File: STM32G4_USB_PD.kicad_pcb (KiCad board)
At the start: 2 copper layers, 34 x 24 mm, 22 parts, among them J1 USB4105-GF-A, J2 8.06.16_J-LINK_6-PIN_NEEDLE_A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, J3 Conn_01x04, J4 Conn_01x02, Q1 2N7002K, U1 STM32G431C8T6, U2 AP2205-W5-7

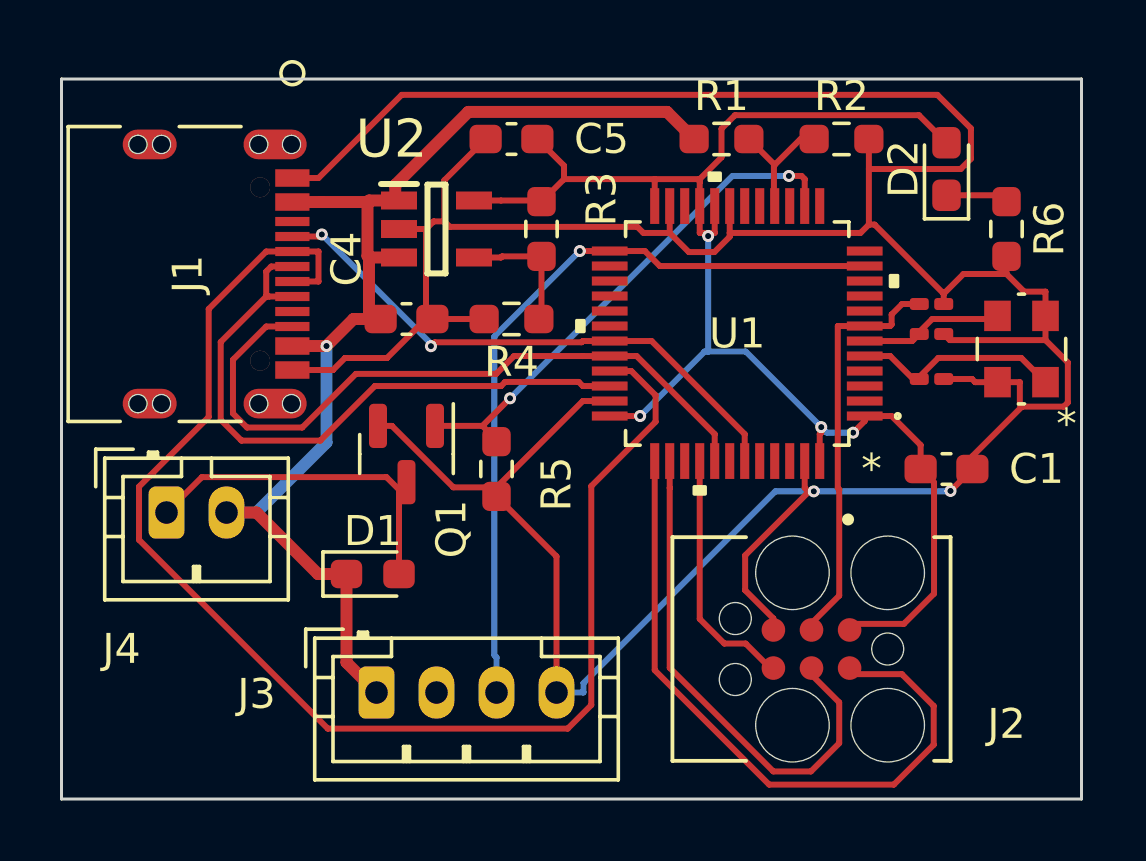
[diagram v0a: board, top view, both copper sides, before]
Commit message: Thicker Trace for VBUS
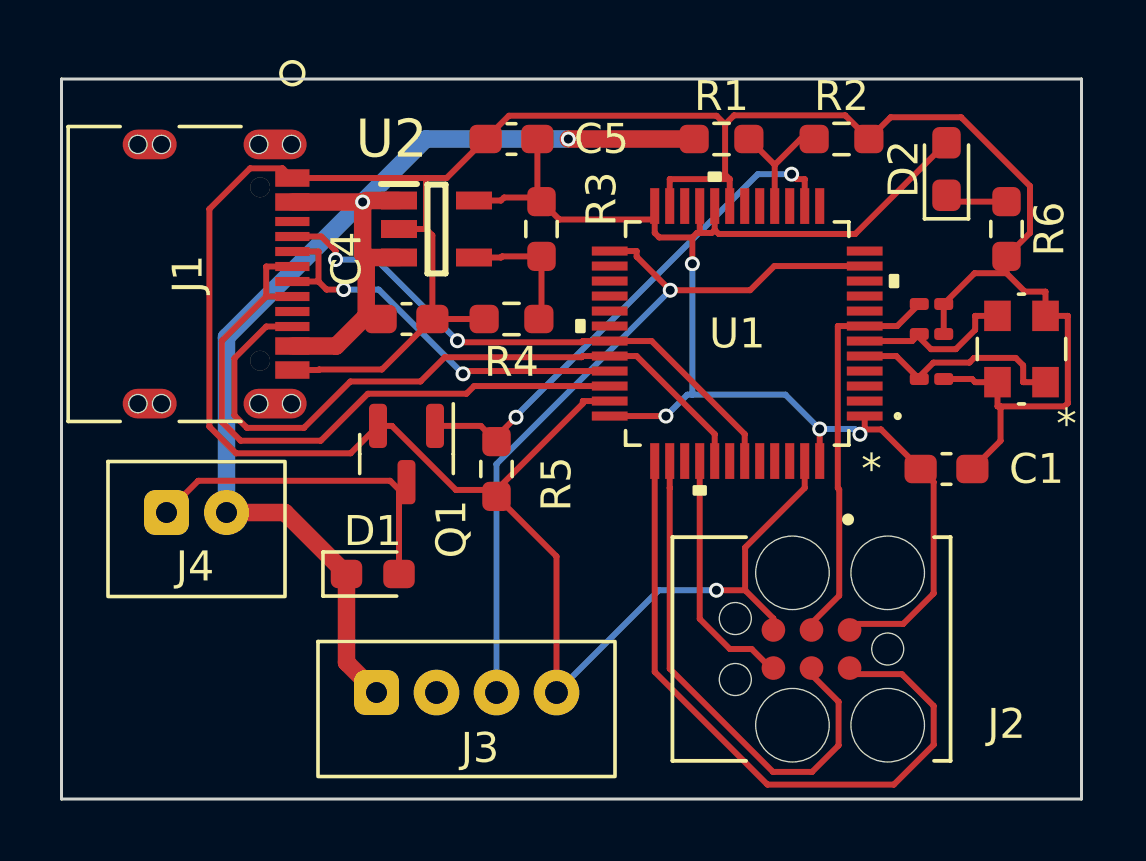
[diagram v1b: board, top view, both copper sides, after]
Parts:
- J3: footprint Connector_JST:JST_PH_B4B-PH-K_1x04_P2.00mm_Vertical -> Anh_Nguyen:JST_PH_2mm_4
- J4: footprint Connector_JST:JST_PH_B2B-PH-K_1x02_P2.00mm_Vertical -> Anh_Nguyen:JST_PH_2mm_2
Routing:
- net USB_D-: track 46.1 -> 13.8 mm, vias 0 -> 2
- net GND: track 128.7 -> 115.1 mm, vias 2 -> 1
- net V_USB: track 40.4 -> 45.3 mm, vias 1 -> 2
- net +3.3V: track 50.4 -> 48.3 mm
- net OSC_OUT: track 4.81 -> 5.50 mm

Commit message: improve VBUS trace width
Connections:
- J1 pad 13: (no net) -> GND
- J1 pad 14: (no net) -> GND
- J1 pad 15: (no net) -> GND
- J1 pad 16: (no net) -> GND
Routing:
- net V_USB: track 45.3 -> 57.0 mm, vias 2 -> 4
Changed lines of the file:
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@@
     (attr smd)
     (fp_text reference "R1" (at 0 -1.43) (layer "F.SilkS")
-      (effects (font (size 1 1) (thickness 0.15)))
+      (effects (font (size 0.5 0.5) (thickness 0.125)))
     )
     (fp_text value "20k" (at 0 1.43) (layer "F.Fab")
@@
       (effects (font (size 1 1) (thickness 0.15)))
     )
-    (fp_circle (center -6.6929 -3.4858) (end -6.3119 -3.4858) (layer "B.SilkS") (width 0.12) (fill none))
     (fp_line (start 4.9149 0.286826) (end 4.9149 -1.776026) (layer "F.SilkS") (width 0.12))
     (fp_line (start 4.9149 3.9878) (end 4.9149 2.251574) (layer "F.SilkS") (width 0.12))
@@
     (fp_line (start -4.9149 2.251574) (end -4.9149 3.9878) (layer "F.SilkS") (width 0.12))
     (fp_line (start -4.9149 3.9878) (end 4.9149 3.9878) (layer "F.SilkS") (width 0.12))
-    (fp_circle (center -6.6929 -3.4858) (end -6.3119 -3.4858) (layer "F.SilkS") (width 0.12) (fill none))
     (fp_line (start -5.069301 4.1148) (end 5.069301 4.1148) (layer "F.CrtYd") (width 0.05))
     (fp_line (start 5.069301 -4.3113) (end -5.069301 -4.3113) (layer "F.CrtYd") (width 0.05))
@@
     (fp_line (start 4.7879 3.8608) (end 4.7879 -3.8608) (layer "F.Fab") (width 0.1))
     (fp_line (start -4.7879 -3.8608) (end -4.7879 3.8608) (layer "F.Fab") (width 0.1))
-    (fp_circle (center -3.2 -5.3908) (end -2.819 -5.3908) (layer "F.Fab") (width 0.1) (fill none))
-    (pad "" np_thru_hole circle (at -4.32 0.8755 270) (size 0.6096 0.6096) (drill 0.6096) (layers *.Cu *.Mask))
-    (pad "" np_thru_hole circle (at 4.32 -3.4569 270) (size 0.6096 0.6096) (drill 0.6096) (layers *.Cu *.Mask))
-    (pad "" np_thru_hole circle (at 4.32 -2.3647 270) (size 0.6096 0.6096) (drill 0.6096) (layers *.Cu *.Mask))
-    (pad "" np_thru_hole circle (at 4.32 1.6629 270) (size 0.6096 0.6096) (drill 0.6096) (layers *.Cu *.Mask))
-    (pad "" np_thru_hole circle (at -4.32 1.6629 270) (size 0.6096 0.6096) (drill 0.6096) (layers *.Cu *.Mask))
-    (pad "" np_thru_hole circle (at 4.32 0.8755 270) (size 0.6096 0.6096) (drill 0.6096) (layers *.Cu *.Mask))
-    (pad "" np_thru_hole circle (at -4.320002 -3.4569 270) (size 0.6096 0.6096) (drill 0.6096) (layers *.Cu *.Mask))
-    (pad "" np_thru_hole circle (at -4.320002 -2.3647 270) (size 0.6096 0.6096) (drill 0.6096) (layers *.Cu *.Mask))
-    (pad "13" smd oval (at -4.320002 1.2692 270) (size 0.9906 1.8034) (layers "F.Cu" "F.Paste" "F.Mask"))
-    (pad "14" smd oval (at 4.320002 1.2692 270) (size 0.9906 1.8034) (layers "F.Cu" "F.Paste" "F.Mask"))
-    (pad "15" smd oval (at -4.320002 -2.9108 270) (size 0.9906 2.1082) (layers "F.Cu" "F.Paste" "F.Mask"))
-    (pad "16" smd oval (at 4.320002 -2.9108 270) (size 0.9906 2.1082) (layers "F.Cu" "F.Paste" "F.Mask"))
-    (pad "17" thru_hole circle (at -2.889999 -2.410801 270) (size 0.6604 0.6604) (drill 0.6604) (layers *.Cu *.Mask))
-    (pad "18" thru_hole circle (at 2.889999 -2.410801 270) (size 0.6604 0.6604) (drill 0.6604) (layers *.Cu *.Mask))
+    (pad "" np_thru_hole circle (at -2.889999 -2.410801 270) (size 0.6604 0.6604) (drill 0.6604) (layers F&B.Cu *.Mask))
+    (pad "" np_thru_hole circle (at 2.889999 -2.410801 270) (size 0.6604 0.6604) (drill 0.6604) (layers F&B.Cu *.Mask))
+    (pad "13" thru_hole oval (at -4.320002 1.2692 270) (size 0.9906 1.8034) (drill oval 0.6 1.4) (layers *.Cu *.Mask)
+      (net 2 "GND") (pinfunction "Shell") (pintype "passive"))
+    (pad "14" thru_hole oval (at 4.320002 1.2692 270) (size 0.9906 1.8034) (drill oval 0.6 1.4) (layers *.Cu *.Mask)
+      (net 2 "GND") (pinfunction "Shell") (pintype "passive"))
+    (pad "15" thru_hole oval (at -4.320002 -2.9108 270) (size 0.9906 2.1082) (drill oval 0.6 1.7) (layers *.Cu *.Mask)
+      (net 2 "GND") (pinfunction "Shell") (pintype "passive"))
+    (pad "16" thru_hole oval (at 4.320002 -2.9108 270) (size 0.9906 2.1082) (drill oval 0.6 1.7) (layers *.Cu *.Mask)
+      (net 2 "GND") (pinfunction "Shell") (pintype "passive"))
     (pad "A1-B12" smd rect (at -3.2 -3.4858 270) (size 0.5842 1.143) (layers "F.Cu" "F.Paste" "F.Mask")
       (net 2 "GND") (pinfunction "GND") (pintype "power_in"))
@@
     (attr smd)
     (fp_text reference "R2" (at 0 -1.43) (layer "F.SilkS")
-      (effects (font (size 1 1) (thickness 0.15)))
+      (effects (font (size 0.5 0.5) (thickness 0.125)))
     )
     (fp_text value "3.6k" (at 0 1.43) (layer "F.Fab")
@@
   (segment (start 96.0386 73.331) (end 96.1576 73.45) (width 0.5842) (layer "F.Cu") (net 4))
   (segment (start 96.1576 75.3991) (end 95.1567 76.4) (width 0.5842) (layer "F.Cu") (net 4))
-  (segment (start 95.1567 76.4) (end 93.6952 76.4) (width 0.5842) (layer "F.Cu") (net 4))
+  (segment (start 95.1567 76.4) (end 95 76.4) (width 0.5842) (layer "F.Cu") (net 4))
   (segment (start 96.0386 71.6) (end 96.0386 73.331) (width 0.5842) (layer "F.Cu") (net 4))
   (segment (start 96.2585 75.5) (end 96.1576 75.3991) (width 0.5842) (layer "F.Cu") (net 4))
-  (segment (start 93.45 81.95) (end 95.5 84) (width 0.5842) (layer "F.Cu") (net 4))
+  (segment (start 93.45 81.95) (end 95.5 84) (width 1.4) (layer "F.Cu") (net 4))
   (segment (start 107.0875 69.5) (end 102.8933 69.5) (width 0.5842) (layer "F.Cu") (net 4))
   (segment (start 96.1576 71.55) (end 96.1076 71.6) (width 0.5842) (layer "F.Cu") (net 4))
   (segment (start 97.25 71.55) (end 96.1576 71.55) (width 0.5842) (layer "F.Cu") (net 4))
-  (segment (start 95.5 86.95) (end 96.5 87.95) (width 0.5842) (layer "F.Cu") (net 4))
-  (segment (start 95.5 84) (end 95.5 86.95) (width 0.5842) (layer "F.Cu") (net 4))
+  (segment (start 95.5 86.95) (end 96.5 87.95) (width 1.4) (layer "F.Cu") (net 4))
+  (segment (start 95.5 84) (end 95.5 86.95) (width 1.4) (layer "F.Cu") (net 4))
+  (segment (start 95.2 71.6) (end 93.6952 71.6) (width 0.5842) (layer "F.Cu") (net 4))
+  (segment (start 95.2 71.6) (end 96.0386 71.6) (width 0.5842) (layer "F.Cu") (net 4))
   (segment (start 97.25 73.45) (end 96.1576 73.45) (width 0.5842) (layer "F.Cu") (net 4))
   (segment (start 96.1576 75.3991) (end 96.1576 73.45) (width 0.5842) (layer "F.Cu") (net 4))
   (segment (start 96.1076 71.6) (end 96.0386 71.6) (width 0.5842) (layer "F.Cu") (net 4))
   (segment (start 96.6375 75.5) (end 96.2585 75.5) (width 0.5842) (layer "F.Cu") (net 4))
-  (segment (start 96.0386 71.6) (end 93.6952 71.6) (width 0.5842) (layer "F.Cu") (net 4))
-  (segment (start 91.5 81.95) (end 93.45 81.95) (width 0.5842) (layer "F.Cu") (net 4))
-  (via (at 96.0386 71.6) (size 0.5) (drill 0.3) (layers "F.Cu" "B.Cu") (net 4))
+  (segment (start 91.5 81.95) (end 93.45 81.95) (width 1.4) (layer "F.Cu") (net 4))
+  (segment (start 95 76.4) (end 93.6952 76.4) (width 0.5842) (layer "F.Cu") (net 4))
+  (via (at 95.2 71.6) (size 0.6) (drill 0.4) (layers "F.Cu" "B.Cu") (net 4))
+  (via (at 95 76.4) (size 0.6) (drill 0.4) (layers "F.Cu" "B.Cu") (net 4))
+  (via (at 96.0386 71.6) (size 0.6) (drill 0.4) (layers "F.Cu" "B.Cu") (net 4))
   (via (at 102.8933 69.5) (size 0.5) (drill 0.3) (layers "F.Cu" "B.Cu") (net 4))
-  (segment (start 91.5 76.1043) (end 91.5 81.95) (width 0.5842) (layer "B.Cu") (net 4))
+  (segment (start 90.95 79.11777) (end 91.5 79.66777) (width 1.4) (layer "B.Cu") (net 4))
+  (segment (start 91.5 82.95) (end 96.5 87.95) (width 1.4) (layer "B.Cu") (net 4))
+  (segment (start 90.95 75.85) (end 90.95 79.11777) (width 1.4) (layer "B.Cu") (net 4))
+  (segment (start 95 76.4) (end 93.10215 74.50215) (width 0.5842) (layer "B.Cu") (net 4))
+  (segment (start 95.2 71.6) (end 90.95 75.85) (width 1.4) (layer "B.Cu") (net 4))
+  (segment (start 91.5 79.66777) (end 91.5 81.95) (width 1.4) (layer "B.Cu") (net 4))
   (segment (start 96.0386 71.6) (end 96.0043 71.6) (width 0.5842) (layer "B.Cu") (net 4))
   (segment (start 96.0386 71.6) (end 98.1386 69.5) (width 0.5842) (layer "B.Cu") (net 4))
-  (segment (start 96.0043 71.6) (end 91.5 76.1043) (width 0.5842) (layer "B.Cu") (net 4))
+  (segment (start 95.2 71.6) (end 96.0386 71.6) (width 1.4) (layer "B.Cu") (net 4))
+  (segment (start 91.5 81.95) (end 91.5 82.95) (width 1.4) (layer "B.Cu") (net 4))
   (segment (start 98.1386 69.5) (end 102.8933 69.5) (width 0.5842) (layer "B.Cu") (net 4))
   (segment (start 107.6737 72.6314) (end 107.2738 72.6314) (width 0.2) (layer "F.Cu") (net 5))
@@
   (segment (start 90.558 80.892) (end 89.5 81.95) (width 0.2) (layer "F.Cu") (net 44))
   (zone (net 2) (net_name "GND") (layers F&B.Cu) (name "GND") (hatch edge 0.508)
-    (connect_pads (clearance 0.508))
+    (connect_pads yes (clearance 0.508))
     (min_thickness 0.254) (filled_areas_thickness no)
     (fill yes (thermal_gap 0.508) (thermal_bridge_width 0.508) (smoothing fillet) (radius 0.1))
